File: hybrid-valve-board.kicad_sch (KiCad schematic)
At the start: 40 parts, among them J1 XV Supply, J10 ARM, J2 MCU Supply, J3 XV In, J4 XV In, J5 XV In, J6 Continuity, J7 XV Out, J8 XV Out, J9 XV Out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

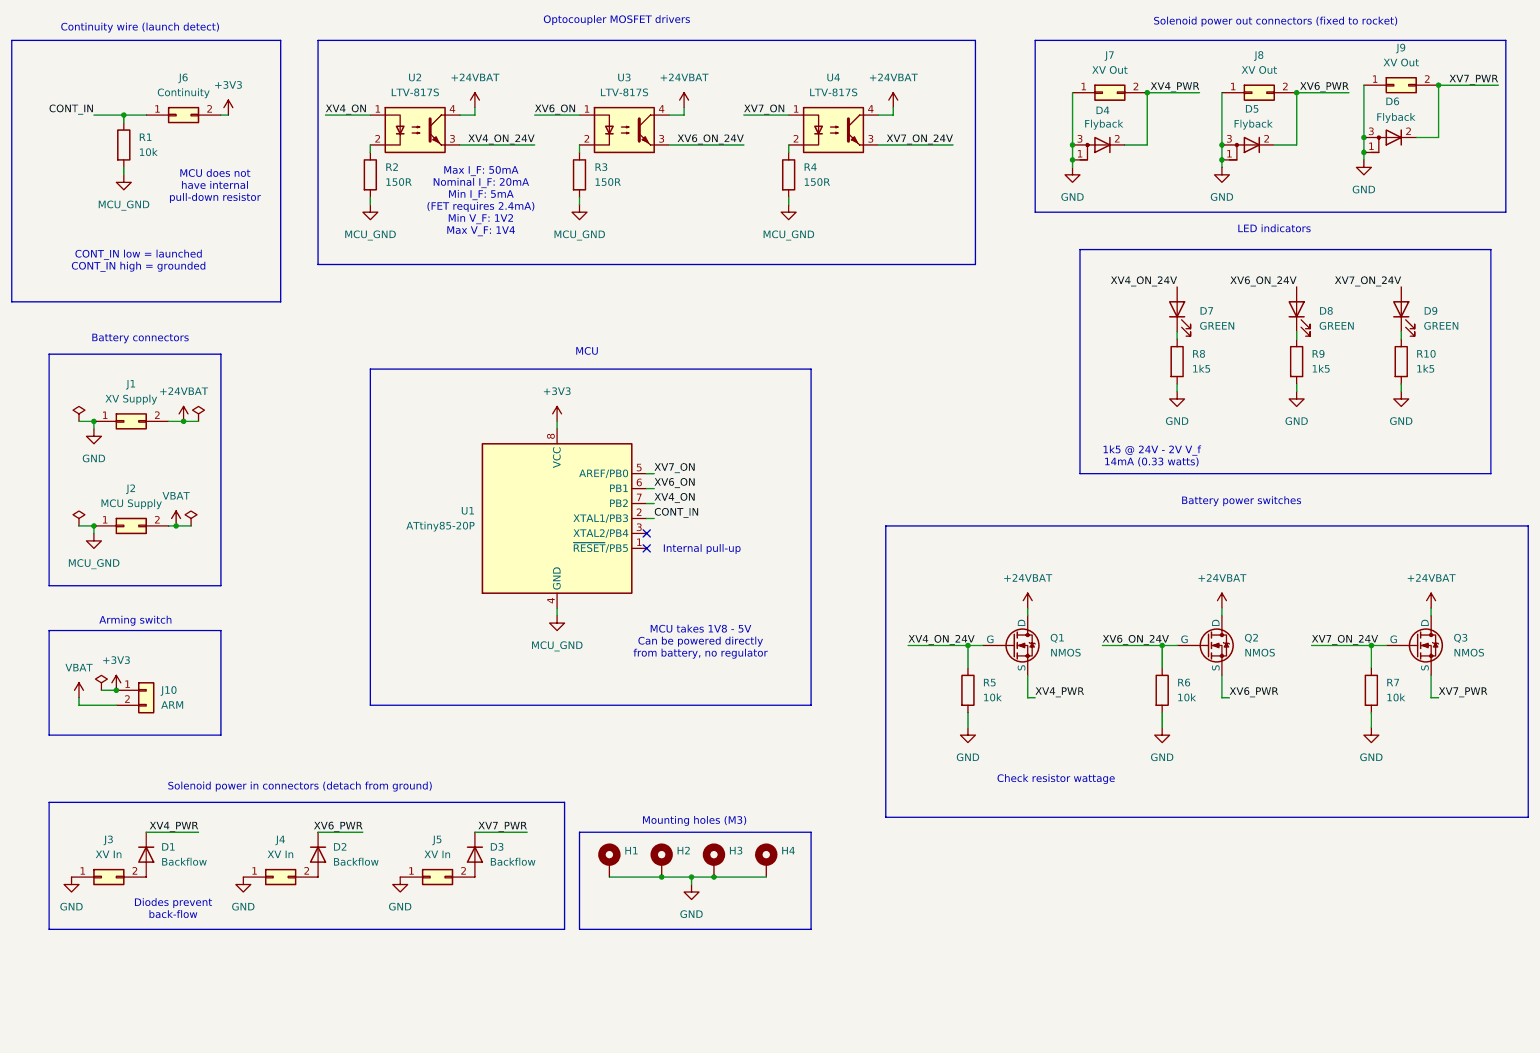
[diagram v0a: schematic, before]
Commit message: Added: reverse polarity protection for MCU, arming LED and PMOS switching
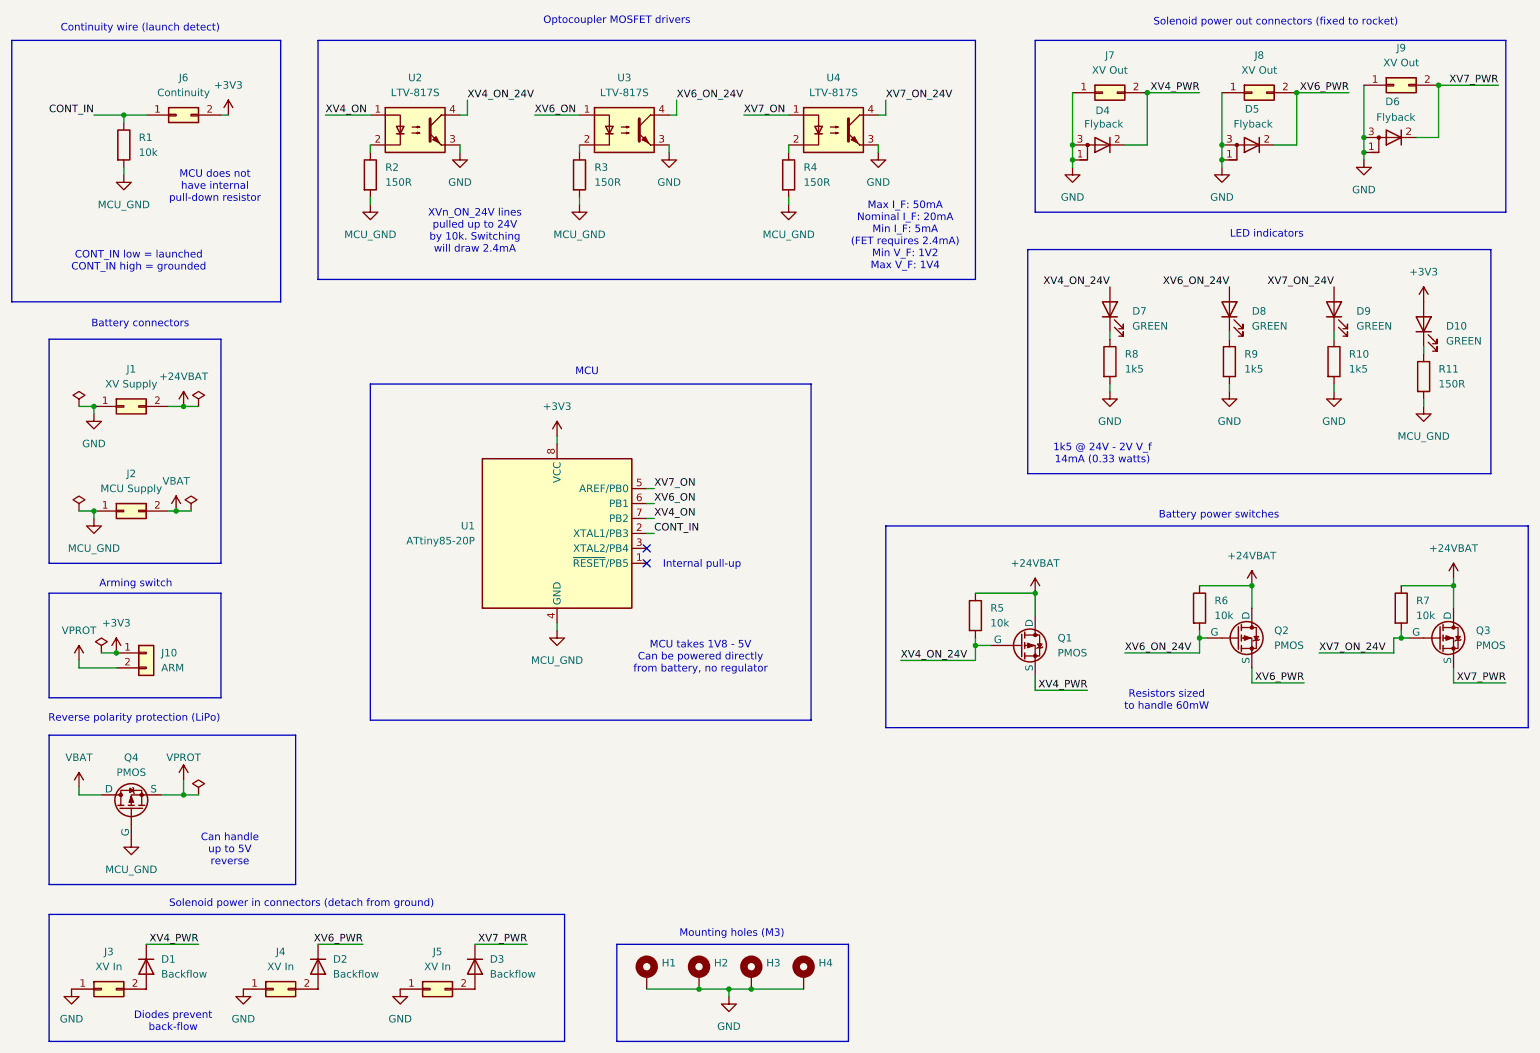
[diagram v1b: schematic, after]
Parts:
- removed Q1, Q2, Q3: NMOS, Package_TO_SOT_SMD:TO-252-2, symbol Simulation_SPICE:NMOS
- added D10: GREEN, LED_SMD:LED_0805_2012Metric_Pad1.15x1.40mm_HandSolder, symbol Device:LED
- added Q1, Q2, Q3: PMOS, Package_TO_SOT_SMD:TO-252-2, symbol Simulation_SPICE:PMOS
- added Q4: PMOS, Package_TO_SOT_SMD:SOT-23-3, symbol Simulation_SPICE:PMOS
- added R11: 150R, Resistor_SMD:R_0805_2012Metric_Pad1.20x1.40mm_HandSolder, symbol Device:R
- R2, R3, R4: MPN RK73B2ATTDD151J -> RK73B2ATTDD151J
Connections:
- net +24VBAT: now also R5.1, R6.1, R7.1, Q1.2 (D), Q2.2 (D), Q3.2 (D); no longer U2.4, U3.4, U4.4
- net +3V3: now also D10.2 (A)
- net GND: now also U2.3, U3.3, U4.3; no longer R5.2, R6.2, R7.2
- net MCU_GND: now also Q4.1 (G), R11.2
- net VBAT: now also Q4.3 (D); no longer J10.2 (Pin_2)
- net XV4_ON_24V: now also R5.2, U2.4, Q1.1 (G); no longer R5.1, U2.3
- net XV4_PWR: now also Q1.3 (S)
- net XV6_ON_24V: now also R6.2, U3.4, Q2.1 (G); no longer R6.1, U3.3
- net XV6_PWR: now also Q2.3 (S)
- net XV7_ON_24V: now also R7.2, U4.4, Q3.1 (G); no longer R7.1, U4.3
- net XV7_PWR: now also Q3.3 (S)
- new net: D10.1 (K), R11.1
- new net VPROT: J10.2 (Pin_2), Q4.2 (S)
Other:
- note added: "Can handle up to 5V reverse"
- note added: "Resistors sized to handle 60mW"
- note added: "Reverse polarity protection (LiPo)"
- note added: "XVn_ON_24V lines pulled up to 24V by 10k. Switching will draw 2.4mA"
- note removed: "Check resistor wattage"
- moved on the sheet: D1, D2, D3, D7, D8, D9, H1, H2, H3, H4, J1, J10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

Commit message: Update BOM
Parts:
- D4, D5, D6: MPN (none) -> RFN10NS4STL
- J1, J2, J3, J4, J5, J6, J7, J8, J9: MPN (none) -> 172648-0102
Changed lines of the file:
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@@
 			)
 		)
-		(property "Datasheet" "~"
+		(property "Datasheet" "https://fscdn.rohm.com/en/products/databook/datasheet/discrete/diode/fast_recovery/rfn10ns4s.pdf"
 			(at 209.55 43.18 0)
 			(effects
@@
 			)
 		)
+		(property "MPN" "RFN10NS4STL"
+			(at 209.55 43.18 0)
+			(effects
+				(font
+					(size 1.27 1.27)
+				)
+				(hide yes)
+			)
+		)
 		(pin "3"
 		)
@@
 			)
 		)
+		(property "MPN" "~"
+			(at 132.08 184.15 0)
+			(effects
+				(font
+					(size 1.27 1.27)
+				)
+				(hide yes)
+			)
+		)
 		(pin "1"
 		)
@@
 			)
 		)
+		(property "MPN" "~"
+			(at 158.75 184.15 0)
+			(effects
+				(font
+					(size 1.27 1.27)
+				)
+				(hide yes)
+			)
+		)
 		(pin "1"
 		)
@@
 			)
 		)
+		(property "MPN" "172648-0102"
+			(at 259.08 33.02 0)
+			(effects
+				(font
+					(size 1.27 1.27)
+				)
+				(hide yes)
+			)
+		)
 		(pin "2"
 		)
@@
 			)
 		)
+		(property "MPN" "172648-0102"
+			(at 68.58 186.69 0)
+			(effects
+				(font
+					(size 1.27 1.27)
+				)
+				(hide yes)
+			)
+		)
 		(pin "2"
 		)
@@
 			)
 		)
+		(property "MPN" "~"
+			(at 149.86 184.15 0)
+			(effects
+				(font
+					(size 1.27 1.27)
+				)
+				(hide yes)
+			)
+		)
 		(pin "1"
 		)
@@
 			)
 		)
-		(property "Datasheet" "~"
+		(property "Datasheet" "https://fscdn.rohm.com/en/products/databook/datasheet/discrete/diode/fast_recovery/rfn10ns4s.pdf"
 			(at 234.95 43.18 0)
 			(effects
@@
 			)
 		)
+		(property "MPN" "RFN10NS4STL"
+			(at 234.95 43.18 0)
+			(effects
+				(font
+					(size 1.27 1.27)
+				)
+				(hide yes)
+			)
+		)
 		(pin "3"
 		)
@@
 			)
 		)
+		(property "MPN" "172648-0102"
+			(at 209.55 34.29 0)
+			(effects
+				(font
+					(size 1.27 1.27)
+				)
+				(hide yes)
+			)
+		)
 		(pin "2"
 		)
@@
 			)
 		)
+		(property "MPN" "~"
+			(at 140.97 184.15 0)
+			(effects
+				(font
+					(size 1.27 1.27)
+				)
+				(hide yes)
+			)
+		)
 		(pin "1"
 		)
@@
 			)
 		)
-		(property "Datasheet" "https://www.mouser.ca/manufacturer/rohm-semiconductor/"
+		(property "Datasheet" "https://www.koaspeer.com/pdfs/RK73B.pdf"
 			(at 264.16 82.55 0)
 			(effects
@@
 			)
 		)
+		(property "MPN" "172648-0102"
+			(at 43.18 105.41 0)
+			(effects
+				(font
+					(size 1.27 1.27)
+				)
+				(hide yes)
+			)
+		)
 		(pin "2"
 		)
@@
 			)
 		)
+		(property "MPN" "172648-0102"
+			(at 234.95 34.29 0)
+			(effects
+				(font
+					(size 1.27 1.27)
+				)
+				(hide yes)
+			)
+		)
 		(pin "2"
 		)
@@
 			)
 		)
-		(property "Datasheet" "~"
+		(property "Datasheet" "https://fscdn.rohm.com/en/products/databook/datasheet/discrete/diode/fast_recovery/rfn10ns4s.pdf"
 			(at 259.08 41.91 0)
 			(effects
@@
 			)
 		)
+		(property "MPN" "RFN10NS4STL"
+			(at 259.08 41.91 0)
+			(effects
+				(font
+					(size 1.27 1.27)
+				)
+				(hide yes)
+			)
+		)
 		(pin "3"
 		)
@@
 			)
 		)
+		(property "MPN" "172648-0102"
+			(at 95.25 186.69 0)
+			(effects
+				(font
+					(size 1.27 1.27)
+				)
+				(hide yes)
+			)
+		)
 		(pin "2"
 		)
@@
 			)
 		)
+		(property "MPN" "172648-0102"
+			(at 52.07 38.1 0)
+			(effects
+				(font
+					(size 1.27 1.27)
+				)
+				(hide yes)
+			)
+		)
 		(pin "2"
 		)
@@
 			)
 		)
+		(property "MPN" "172648-0102"
+			(at 43.18 87.63 0)
+			(effects
+				(font
+					(size 1.27 1.27)
+				)
+				(hide yes)
+			)
+		)
 		(pin "2"
 		)
@@
 			(at 39.37 186.69 0)
 			(effects
+				(font
+					(size 1.27 1.27)
+				)
+				(hide yes)
+			)
+		)
+		(property "MPN" "172648-0102"
+			(at 39.37 186.69 0)
+			(effects

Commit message: Update backflow diodes to identical package that can handle 1.5A at 75C
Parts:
- D1, D2, D3: MPN RF201LAM4STR -> RBR3LAM60BTR
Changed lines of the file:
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@@
 			)
 		)
-		(property "MPN" "RF201LAM4STR"
+		(property "MPN" "RBR3LAM60BTR"
 			(at 102.87 182.88 0)
 			(effects
@@
 			)
 		)
-		(property "MPN" "RF201LAM4STR"
+		(property "MPN" "RBR3LAM60BTR"
 			(at 76.2 182.88 0)
 			(effects
@@
 			)
 		)
-		(property "MPN" "RF201LAM4STR"
+		(property "MPN" "RBR3LAM60BTR"
 			(at 46.99 182.88 0)
 			(effects

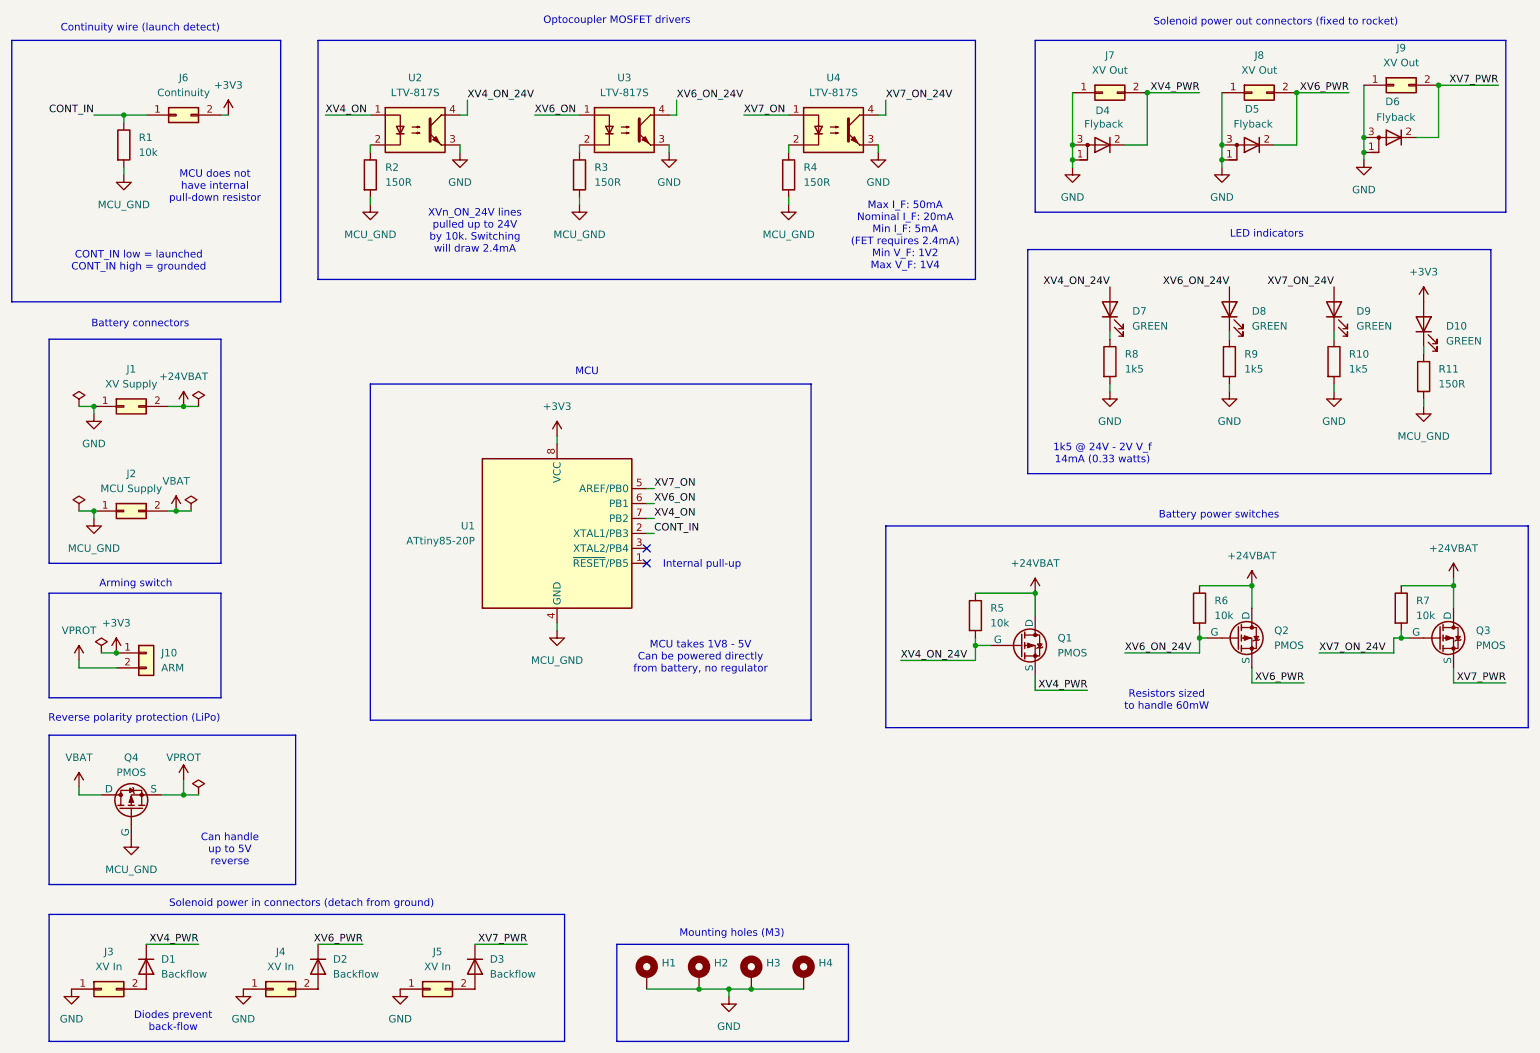
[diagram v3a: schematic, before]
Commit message: Added power decoupling capacitors for MCU
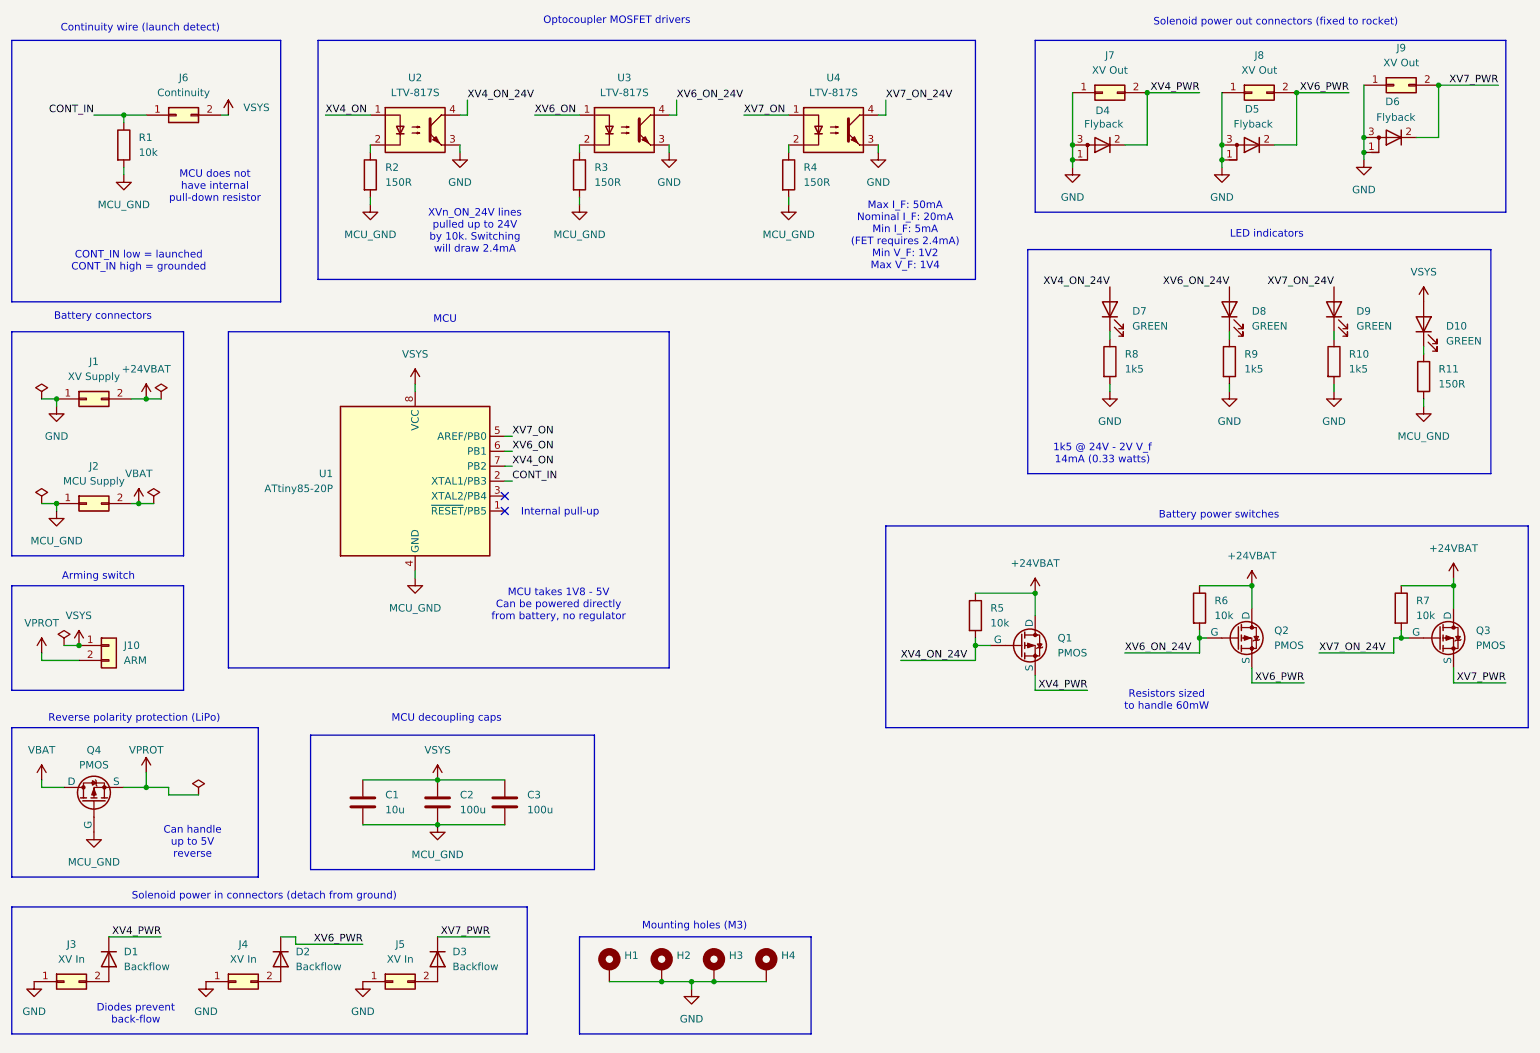
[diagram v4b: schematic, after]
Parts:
- added C1: 10u, Capacitor_SMD:C_0805_2012Metric, symbol Device:C
- added C2, C3: 100u, Capacitor_SMD:C_0805_2012Metric, symbol Device:C
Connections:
- net MCU_GND: now also C1.2, C2.2, C3.2
- net +3V3 renamed VSYS
- net VSYS: now also C1.1, C2.1, C3.1
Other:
- note added: "MCU decoupling caps"
- moved on the sheet: D1, D2, D3, H1, H2, H3, H4, J1, J10, J2, J3, J4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
